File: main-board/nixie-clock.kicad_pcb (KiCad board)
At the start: 2 copper layers, 54 parts, among them P1 ESP8266_CONN, P2 CONN_01X06, P3 CONN_01X03, P4 CONN_02X05, P5 CONN_02X05, P6 CONN_02X05, P7 CONN_02X05, Q1 2N7002, Q2 2N7002, SW1 ROTARY_ENCODER_SWITCH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

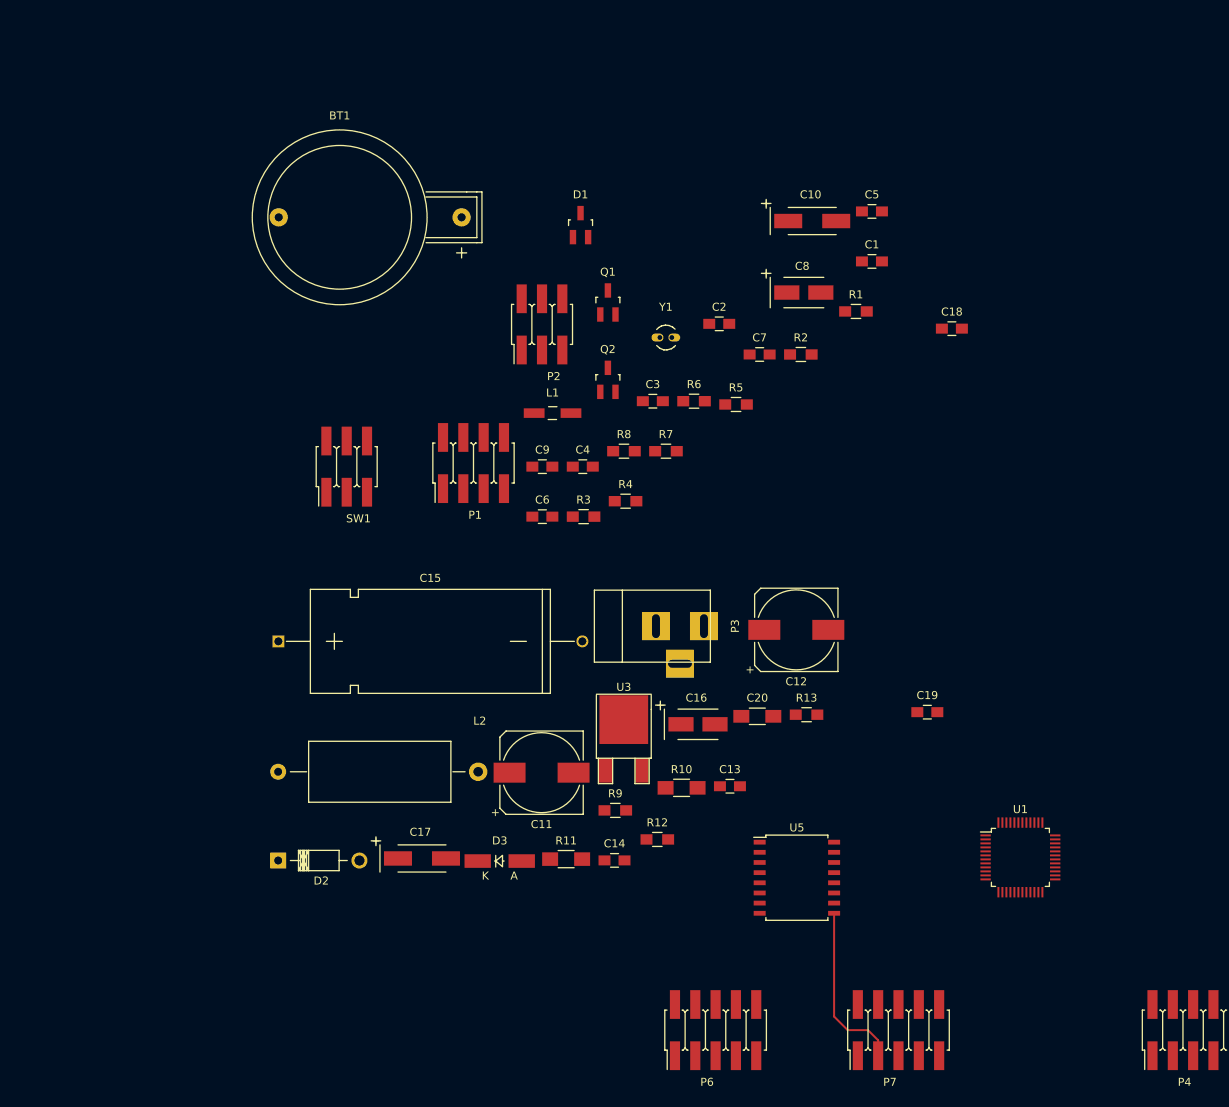
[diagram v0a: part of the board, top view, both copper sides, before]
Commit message: Poprawione polaczenie sciezek; zmiana nazwy wyjscia VDD
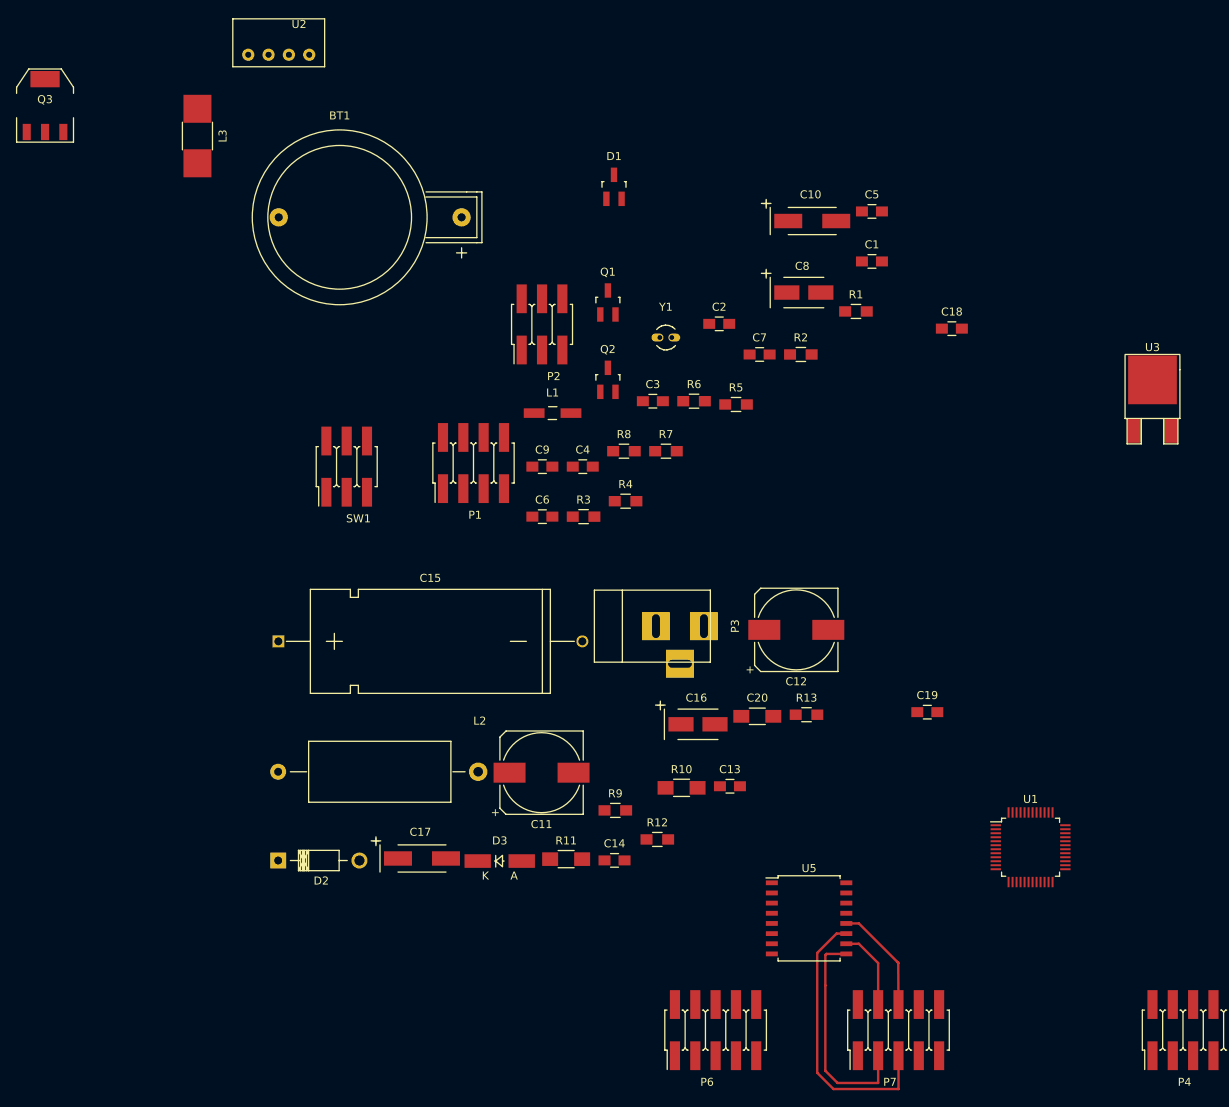
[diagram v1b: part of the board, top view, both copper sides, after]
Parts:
- added L3: 100uH, Resistors_SMD:R_1812_HandSoldering, F.Cu at (48.3, 31.8)
- added Q3: BSP324, TO_SOT_Packages_SMD:SOT-223, F.Cu at (29.2, 27.9)
- added U2: ROM1205S, footprint-local:SIP4, F.Cu at (58.4, 21.6)
- moved U3 78.6 mm to (167.6, 68.6)
- moved D1 6.36 mm to (100.3, 38.1)
- moved U5 5.30 mm to (124.7, 129.5)
- moved U1 1.80 mm to (152.4, 120.7)
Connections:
- C17 pad 1: +5V -> /Power supply/VDDOUT
- D3 pad 2: +5V -> /Power supply/VDDOUT
- R13 pad 1: +5V -> /Power supply/VDDOUT
- U3 pad 2: +5V -> /Power supply/VDDOUT
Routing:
- net /NIXIE Module Connector 2/2C: track 0.00 -> 34.8 mm
- net /NIXIE Module Connector 2/2D: track 0.00 -> 13.9 mm
- net /NIXIE Module Connector 2/2B: track 0.00 -> 10.2 mm
- net /NIXIE Module Connector 2/2A: track 21.6 -> 27.8 mm
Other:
- net class Default: clearance 0.2 -> 0.254; trace_width 0.25 -> 0.3048; via_dia 0.6 -> 0.889; via_drill 0.4 -> 0.635
- net class HV added: clearance 1.27, trace_width 0.635, via_dia 0.889, via_drill 0.635
- net class Zasilanie added: clearance 0.3048, trace_width 0.635, via_dia 0.889, via_drill 0.635
- rule trace_clearance: 0.2 -> 0.254

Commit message: usunięcie błędnego połączenia VDD z +5V
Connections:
- net /200VDC renamed /NIXIE Module Connector 2/200VDC
- net /200VSENSE renamed /Power supply/200VSENSE
- net /BRIGHT_PWM renamed /Power supply/BRIGHT_PWM
- net /NMOD_SCL renamed /NIXIE Module Connector 2/SCL
- net /NMOD_SDA renamed /NIXIE Module Connector 2/SDA
- C10 pad 1: +5V -> VDD
- C17 pad 1: /Power supply/VDDOUT -> VDD
- C5 pad 2: +5V -> VDD
- C6 pad 2: +5V -> VDD
- C7 pad 2: +5V -> VDD
- C8 pad 1: +5V -> VDD
- D1 pad 2: +5V -> VDD
- D3 pad 2: /Power supply/VDDOUT -> VDD
- L1 pad 1: +5V -> VDD
- P1 pad 4: Net-(P1-Pad4) -> (no net)
- P1 pad 5: +5V -> VDD
- P1 pad 6: Net-(P1-Pad6) -> (no net)
- P1 pad 7: +5V -> VDD
- P2 pad 2: +5V -> VDD
- P3 pad 3: Net-(P3-Pad3) -> (no net)
- Q1 pad 2: +5V -> VDD
- Q2 pad 2: +5V -> VDD
- R13 pad 1: /Power supply/VDDOUT -> VDD
- R3 pad 1: +5V -> VDD
- R4 pad 1: +5V -> VDD
- R5 pad 2: +5V -> VDD
- R6 pad 1: +5V -> VDD
- R7 pad 1: +5V -> VDD
- R8 pad 1: +5V -> VDD
- U1 pad 10: Net-(U1-Pad10) -> (no net)
- U1 pad 14: Net-(U1-Pad14) -> (no net)
- U1 pad 15: Net-(U1-Pad15) -> (no net)
- U1 pad 16: Net-(U1-Pad16) -> (no net)
- U1 pad 17: Net-(U1-Pad17) -> (no net)
- U1 pad 18: Net-(U1-Pad18) -> (no net)
- U1 pad 2: Net-(U1-Pad2) -> (no net)
- U1 pad 20: Net-(U1-Pad20) -> (no net)
- U1 pad 22: Net-(U1-Pad22) -> (no net)
- U1 pad 24: +5V -> VDD
- U1 pad 25: Net-(U1-Pad25) -> (no net)
- U1 pad 26: Net-(U1-Pad26) -> (no net)
- U1 pad 27: Net-(U1-Pad27) -> (no net)
- U1 pad 28: Net-(U1-Pad28) -> (no net)
- U1 pad 29: Net-(U1-Pad29) -> (no net)
- U1 pad 33: Net-(U1-Pad33) -> (no net)
- U1 pad 36: +5V -> VDD
- U1 pad 38: Net-(U1-Pad38) -> (no net)
- U1 pad 39: Net-(U1-Pad39) -> (no net)
- U1 pad 40: Net-(U1-Pad40) -> (no net)
- U1 pad 41: Net-(U1-Pad41) -> (no net)
- U1 pad 45: Net-(U1-Pad45) -> (no net)
- U1 pad 46: Net-(U1-Pad46) -> (no net)
- U1 pad 48: +5V -> VDD
- U1 pad 5: Net-(U1-Pad5) -> (no net)
- U1 pad 6: Net-(U1-Pad6) -> (no net)
- U3 pad 2: /Power supply/VDDOUT -> VDD
- U4 pad 13: Net-(U4-Pad13) -> (no net)
- U5 pad 13: Net-(U5-Pad13) -> (no net)
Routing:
- net VDD: track 0.00 -> 11.6 mm

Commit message: Temp
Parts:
- moved C13 114.4 mm to (226.1, 86.4), turned to 180 degrees
- moved C1 113.7 mm to (243.1, 20.8)
- moved C10 113.7 mm to (235.6, 15.7)
- moved C11 113.7 mm to (201.8, 84.7)
- moved C15 113.7 mm to (168.9, 68.2)
- moved C16 113.7 mm to (221.3, 78.6)
- moved C17 113.7 mm to (186.8, 95.4)
- moved C18 113.7 mm to (253.1, 29.2)
- moved C19 113.7 mm to (250.0, 77.1)
- moved C20 113.7 mm to (228.7, 77.6)
- moved C3 113.7 mm to (215.7, 38.2)
- moved C5 113.7 mm to (243.1, 14.5)
- moved C6 113.7 mm to (201.9, 52.7)
- moved C7 113.7 mm to (229.0, 32.4)
- moved C9 113.7 mm to (201.9, 46.4)
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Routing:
- net VDD: track 11.6 -> 0.00 mm
- net (no net): track 0.00 -> 11.6 mm

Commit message: Obrys plytki 40% elementow
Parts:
- C15: footprint Capacitors_ThroughHole:C_Axial_D13_L31_P38 -> Capacitors_ThroughHole:C_Radial_D10_L20_P5
- C20: footprint Capacitors_SMD:C_1206_HandSoldering -> Capacitors_SMD:C_1812_HandSoldering; moved to B.Cu
- D2: footprint Diodes_ThroughHole:Diode_DO-41_SOD81_Horizontal_RM10 -> Diodes_ThroughHole:Diode_DO-41_SOD81_Vertical_AnodeUp
- L2: value 10mH -> 100uH; footprint Choke_Axial_ThroughHole:Choke_Horizontal_RM25mm -> footprint-local:Neosid_Inductor_Sd8
- moved Q3 188.7 mm to (187.0, 131.5), turned to 270 degrees
- moved L3 177.8 mm to (205.1, 115.5), turned to 180 degrees
- moved C19 162.6 mm to (98.7, 136.5), turned to 180 degrees
- moved R1 159.3 mm to (128.7, 140.0), turned to 90 degrees
- moved C5 157.1 mm to (138.0, 131.4), turned to 270 degrees
- moved R2 153.1 mm to (126.6, 141.4), turned to 90 degrees
- moved Q1 137.1 mm to (131.7, 138.4)
- moved U3 134.4 mm to (166.3, 116.4), turned to 180 degrees
- moved P3 128.1 mm to (219.9, 116.0), turned to 270 degrees
- moved Q2 126.0 mm to (137.4, 138.5)
- moved C7 125.4 mm to (140.3, 120.9), turned to 180 degrees
- moved C18 122.5 mm to (201.6, 140.3), turned to 270 degrees
- moved P2 121.9 mm to (130.9, 127.8), turned to 90 degrees
- moved R4 113.4 mm to (140.2, 138.3), turned to 90 degrees
- moved R3 112.2 mm to (134.5, 138.3), turned to 90 degrees
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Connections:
- net /NIXIE Module Connector 2/200VDC renamed /200VDC
- net /NIXIE Module Connector 2/SCL renamed /NMOD_SCL
- net /NIXIE Module Connector 2/SDA renamed /NMOD_SDA
- net /Power supply/200VSENSE renamed /200VSENSE
- net /Power supply/BRIGHT_PWM renamed /BRIGHT_PWM
- P1 pad 4: (no net) -> Net-(P1-Pad4)
- P1 pad 6: (no net) -> Net-(P1-Pad6)
- P3 pad 3: (no net) -> Net-(P3-Pad3)
- P4 pad 1: +5V -> /NIXIE Module Connector/1D
- P4 pad 10: GND -> +5V
- P4 pad 3: /NIXIE Module Connector/1A -> /NIXIE Module Connector/1C
- P4 pad 4: /NIXIE Module Connector/1B -> GND
- P4 pad 5: /NIXIE Module Connector/1C -> /NIXIE Module Connector/1B
- P4 pad 6: /NIXIE Module Connector/1D -> GND
- P4 pad 7: GND -> /NIXIE Module Connector/1A
- P4 pad 9: GND -> Net-(P4-Pad9)
- P5 pad 1: +5V -> /NIXIE Module Connector/2D
- P5 pad 10: GND -> +5V
- P5 pad 3: /NIXIE Module Connector/2A -> /NIXIE Module Connector/2C
- P5 pad 4: /NIXIE Module Connector/2B -> GND
- P5 pad 5: /NIXIE Module Connector/2C -> /NIXIE Module Connector/2B
- P5 pad 6: /NIXIE Module Connector/2D -> GND
- P5 pad 7: GND -> /NIXIE Module Connector/2A
- P5 pad 9: GND -> Net-(P5-Pad9)
- P6 pad 1: +5V -> /NIXIE Module Connector 2/1D
- P6 pad 10: GND -> +5V
- P6 pad 3: /NIXIE Module Connector 2/1A -> /NIXIE Module Connector 2/1C
- P6 pad 4: /NIXIE Module Connector 2/1B -> GND
- P6 pad 5: /NIXIE Module Connector 2/1C -> /NIXIE Module Connector 2/1B
- P6 pad 6: /NIXIE Module Connector 2/1D -> GND
- P6 pad 7: GND -> /NIXIE Module Connector 2/1A
- P6 pad 9: GND -> Net-(P6-Pad9)
- P7 pad 1: +5V -> /NIXIE Module Connector 2/2D
- P7 pad 10: GND -> +5V
- P7 pad 3: /NIXIE Module Connector 2/2A -> /NIXIE Module Connector 2/2C
- P7 pad 4: /NIXIE Module Connector 2/2B -> GND
- P7 pad 5: /NIXIE Module Connector 2/2C -> /NIXIE Module Connector 2/2B
- P7 pad 6: /NIXIE Module Connector 2/2D -> GND
- P7 pad 7: GND -> /NIXIE Module Connector 2/2A
- P7 pad 9: GND -> Net-(P7-Pad9)
- U1 pad 10: (no net) -> Net-(U1-Pad10)
- U1 pad 14: (no net) -> Net-(U1-Pad14)
- U1 pad 15: (no net) -> Net-(U1-Pad15)
- U1 pad 16: (no net) -> Net-(U1-Pad16)
- U1 pad 17: (no net) -> Net-(U1-Pad17)
- U1 pad 18: (no net) -> Net-(U1-Pad18)
- U1 pad 2: (no net) -> Net-(U1-Pad2)
- U1 pad 20: (no net) -> Net-(U1-Pad20)
- U1 pad 22: (no net) -> Net-(U1-Pad22)
- U1 pad 25: (no net) -> Net-(U1-Pad25)
- U1 pad 26: (no net) -> Net-(U1-Pad26)
- U1 pad 27: (no net) -> Net-(U1-Pad27)
- U1 pad 28: (no net) -> Net-(U1-Pad28)
- U1 pad 29: (no net) -> Net-(U1-Pad29)
- U1 pad 33: (no net) -> Net-(U1-Pad33)
- U1 pad 38: (no net) -> Net-(U1-Pad38)
- U1 pad 39: (no net) -> Net-(U1-Pad39)
- U1 pad 40: (no net) -> Net-(U1-Pad40)
- U1 pad 41: (no net) -> Net-(U1-Pad41)
- U1 pad 45: (no net) -> Net-(U1-Pad45)
- U1 pad 46: (no net) -> Net-(U1-Pad46)
- U1 pad 5: (no net) -> Net-(U1-Pad5)
- U1 pad 6: (no net) -> Net-(U1-Pad6)
- U4 pad 13: (no net) -> Net-(U4-Pad13)
- U5 pad 13: (no net) -> Net-(U5-Pad13)
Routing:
- net /200VDC: track 0.00 -> 188.3 mm, vias 0 -> 4
- net /NMOD_SDA: track 0.00 -> 110.7 mm
- net /NMOD_SCL: track 0.00 -> 108.5 mm
- net Net-(C11-Pad1): track 0.00 -> 40.0 mm
- net VDD: track 0.00 -> 33.3 mm
- net /NIXIE Module Connector/1D: track 0.00 -> 29.3 mm
- net /NIXIE Module Connector 2/1D: track 0.00 -> 29.3 mm
- net /NIXIE Module Connector/2A: track 0.00 -> 26.4 mm
- net /NIXIE Module Connector/1C: track 0.00 -> 26.0 mm
- net /NIXIE Module Connector 2/1C: track 0.00 -> 26.0 mm
- net GND: track 0.00 -> 24.4 mm, vias 0 -> 1
- net /NIXIE Module Connector/2B: track 0.00 -> 23.9 mm
- net /NIXIE Module Connector/1B: track 0.00 -> 22.6 mm
- net /NIXIE Module Connector 2/1B: track 0.00 -> 22.6 mm
- net /SWDCLK: track 0.00 -> 20.1 mm
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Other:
- board outline added: 168.7 x 41.1 mm
- net class Default: clearance 0.254 -> 0.2032
- net class HV: via_dia 0.889 -> 1.524; via_drill 0.635 -> 0.889
- net class Zasilanie: via_dia 0.889 -> 1.524; via_drill 0.635 -> 0.889
- rule trace_clearance: 0.254 -> 0.2032

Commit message: Do zrobienia przelotki; elementy rozmieszczone
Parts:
- C4, R10, R11, R9: moved to B.Cu
- moved C10 206.4 mm to (65.7, 132.9)
- moved C1 161.6 mm to (124.2, 130.2), turned to 90 degrees
- moved P1 150.2 mm to (65.5, 124.9), turned to 270 degrees
- moved C8 141.5 mm to (147.8, 136.4), turned to 180 degrees
- moved R5 122.4 mm to (135.5, 120.9)
- moved C2 120.1 mm to (157.5, 128.5)
- moved Y1 118.0 mm to (153.0, 129.3), turned to 90 degrees
- moved C3 109.2 mm to (157.4, 130.6)
- moved R6 102.8 mm to (156.0, 118.0), turned to 90 degrees
- moved C4 102.8 mm to (144.9, 128.3), turned to 270 degrees
- moved R8 102.3 mm to (140.4, 117.5)
- moved R7 100.1 mm to (154.1, 122.0), turned to 180 degrees
- moved D1 95.5 mm to (120.3, 131.4), turned to 270 degrees
- moved BT1 92.9 mm to (107.3, 124.5)
- moved R13 80.1 mm to (170.9, 125.6), turned to 270 degrees
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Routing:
- net +5V: track 20.0 -> 266.2 mm, vias 0 -> 9
- net VDD: track 33.3 -> 179.8 mm, vias 0 -> 2
- net /ESP_STBY: track 0.00 -> 85.3 mm, vias 0 -> 2
- net /ESP_Tx: track 0.00 -> 84.9 mm, vias 0 -> 2
- net /ESP_Rx: track 0.00 -> 77.2 mm
- net /BRIGHT_PWM: track 0.00 -> 77.2 mm, vias 0 -> 2
- net Net-(C1-Pad1): track 0.00 -> 35.9 mm, vias 0 -> 2
- net GND: track 24.4 -> 60.1 mm, vias 1 -> 4
- net /RST: track 0.00 -> 24.0 mm, vias 0 -> 3
- net /200VSENSE: track 0.00 -> 22.4 mm, vias 0 -> 1
- net /PRESS: track 0.00 -> 15.3 mm
- net /B: track 0.00 -> 13.6 mm
- net /A: track 0.00 -> 10.8 mm
- net Net-(C3-Pad1): track 0.00 -> 8.12 mm
- net Net-(BT1-Pad1): track 0.00 -> 7.53 mm
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- added copper zone on B.Cu, net GND
- added copper zone on F.Cu, net GND

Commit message: Do sprawdzenia
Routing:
- net GND: track 60.1 -> 95.6 mm, vias 4 -> 15
- net VDD: track 179.8 -> 196.2 mm, vias 2 -> 3
- net Net-(C16-Pad1): track 4.69 -> 17.6 mm

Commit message: Poprawka - dioda pod napieciem z wiekszym odstepem
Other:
- net class HV2 added: clearance 1.016, trace_width 0.635, via_dia 1.524, via_drill 0.889
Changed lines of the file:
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@@
   (page A4)
   (layers
-    (0 F.Cu signal hide)
-    (31 B.Cu signal)
+    (0 F.Cu signal)
+    (31 B.Cu signal hide)
     (32 B.Adhes user)
     (33 F.Adhes user)
@@
   )
   (setup
-    (last_trace_width 1.524)
+    (last_trace_width 1.016)
     (user_trace_width 0.254)
     (user_trace_width 0.3048)
@@
     (add_net "Net-(C3-Pad1)")
     (add_net "Net-(C9-Pad2)")
-    (add_net "Net-(D2-Pad2)")
     (add_net "Net-(L3-Pad1)")
     (add_net "Net-(P1-Pad4)")
@@
     (uvia_drill 0.127)
     (add_net /200VDC)
+  )
+  (net_class HV2 ""
+    (clearance 1.016)
+    (trace_width 0.635)
+    (via_dia 1.524)
+    (via_drill 0.889)
+    (uvia_dia 0.508)
+    (uvia_drill 0.127)
+    (add_net "Net-(D2-Pad2)")
   )
   (net_class Zasilanie ""
@@
   (segment (start 166.5732 127.92202) (end 167.32122 127.174) (width 1.524) (layer F.Cu) (net 10))
   (segment (start 167.32122 127.174) (end 168.7322 127.174) (width 1.524) (layer F.Cu) (net 10))
-  (segment (start 184.8104 123.6726) (end 184.8104 128.0668) (width 1.524) (layer F.Cu) (net 11))
-  (segment (start 184.8104 128.0668) (end 183.6674 129.2098) (width 1.524) (layer F.Cu) (net 11))
+  (segment (start 184.8104 123.6726) (end 184.8104 128.0668) (width 1.016) (layer F.Cu) (net 11))
+  (segment (start 184.8104 128.0668) (end 183.6674 129.2098) (width 1.016) (layer F.Cu) (net 11))
   (segment (start 184.8104 123.6726) (end 181.5084 123.6726) (width 1.524) (layer F.Cu) (net 11))
   (segment (start 181.5084 123.6726) (end 180.8226 122.9868) (width 1.524) (layer F.Cu) (net 11))

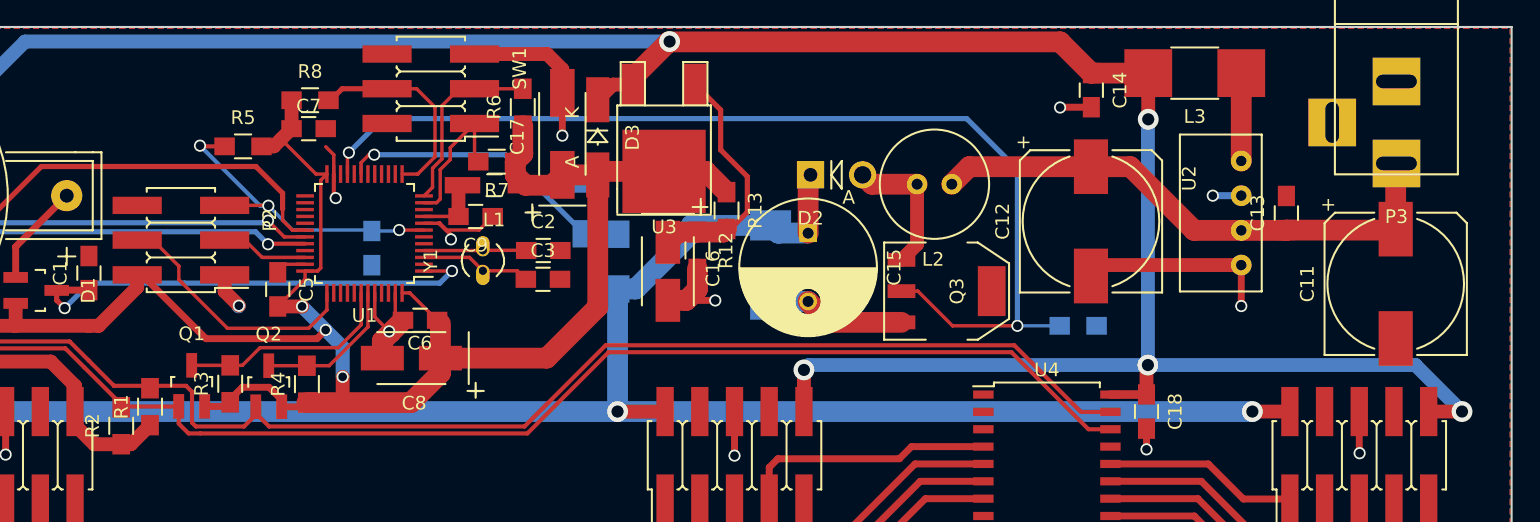
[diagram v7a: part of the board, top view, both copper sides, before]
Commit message: poprawki prowadzenia ścieżek, footprintów, zmniejszenie rozmiaru płytki pod lampę nixie
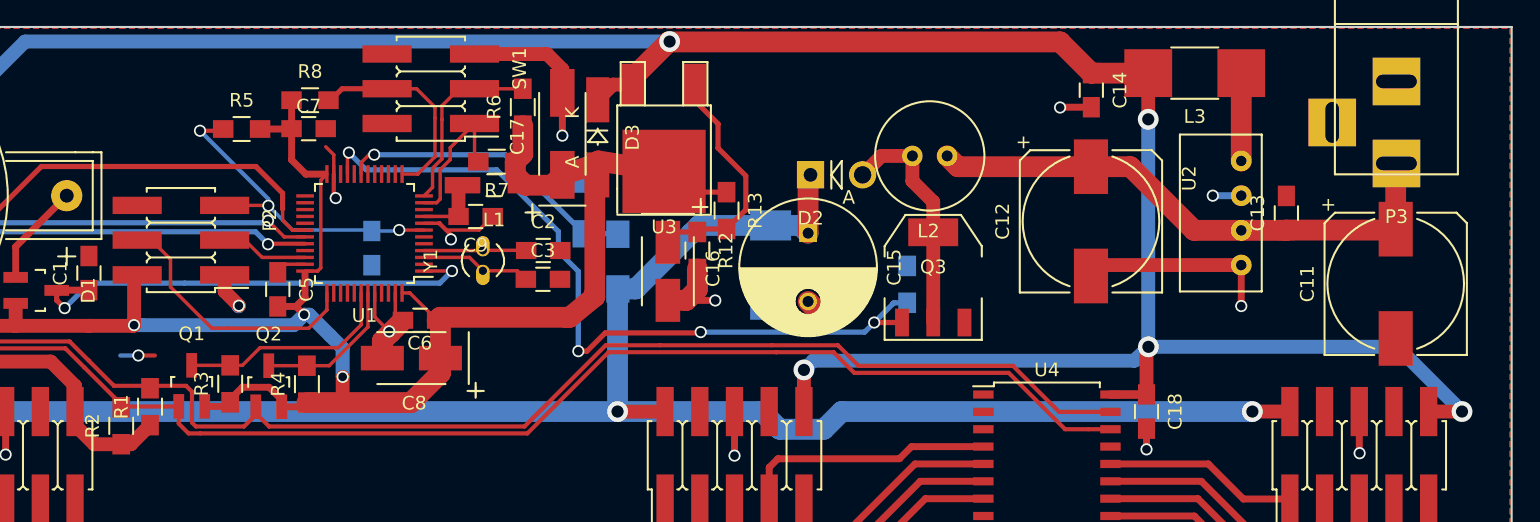
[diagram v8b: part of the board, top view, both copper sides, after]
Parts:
- moved R9 12.9 mm to (184.1, 131.0), turned to 90 degrees
- moved L2 2.10 mm to (185.7, 121.6)
- moved Q3 1.40 mm to (186.0, 130.5), turned to 0 degrees
- moved R5 1.27 mm to (135.4, 119.6)
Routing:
- net /BRIGHT_PWM: track 77.2 -> 56.5 mm, vias 2 -> 4
- net Net-(D2-Pad2): track 10.3 -> 17.0 mm
- net GND: track 95.6 -> 90.0 mm, vias 15 -> 16
- net VDD: track 196.2 -> 193.8 mm
- net /SWDCLK: track 20.1 -> 21.8 mm
- net Net-(C16-Pad1): track 17.6 -> 19.0 mm
- net +5V: track 266.2 -> 267.5 mm
- net /200VDC: track 188.3 -> 189.1 mm
- net /RST: track 24.0 -> 24.7 mm
